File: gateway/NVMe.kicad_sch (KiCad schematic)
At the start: 27 parts, among them IC1501 ST1S14PHR, X1501 SSD

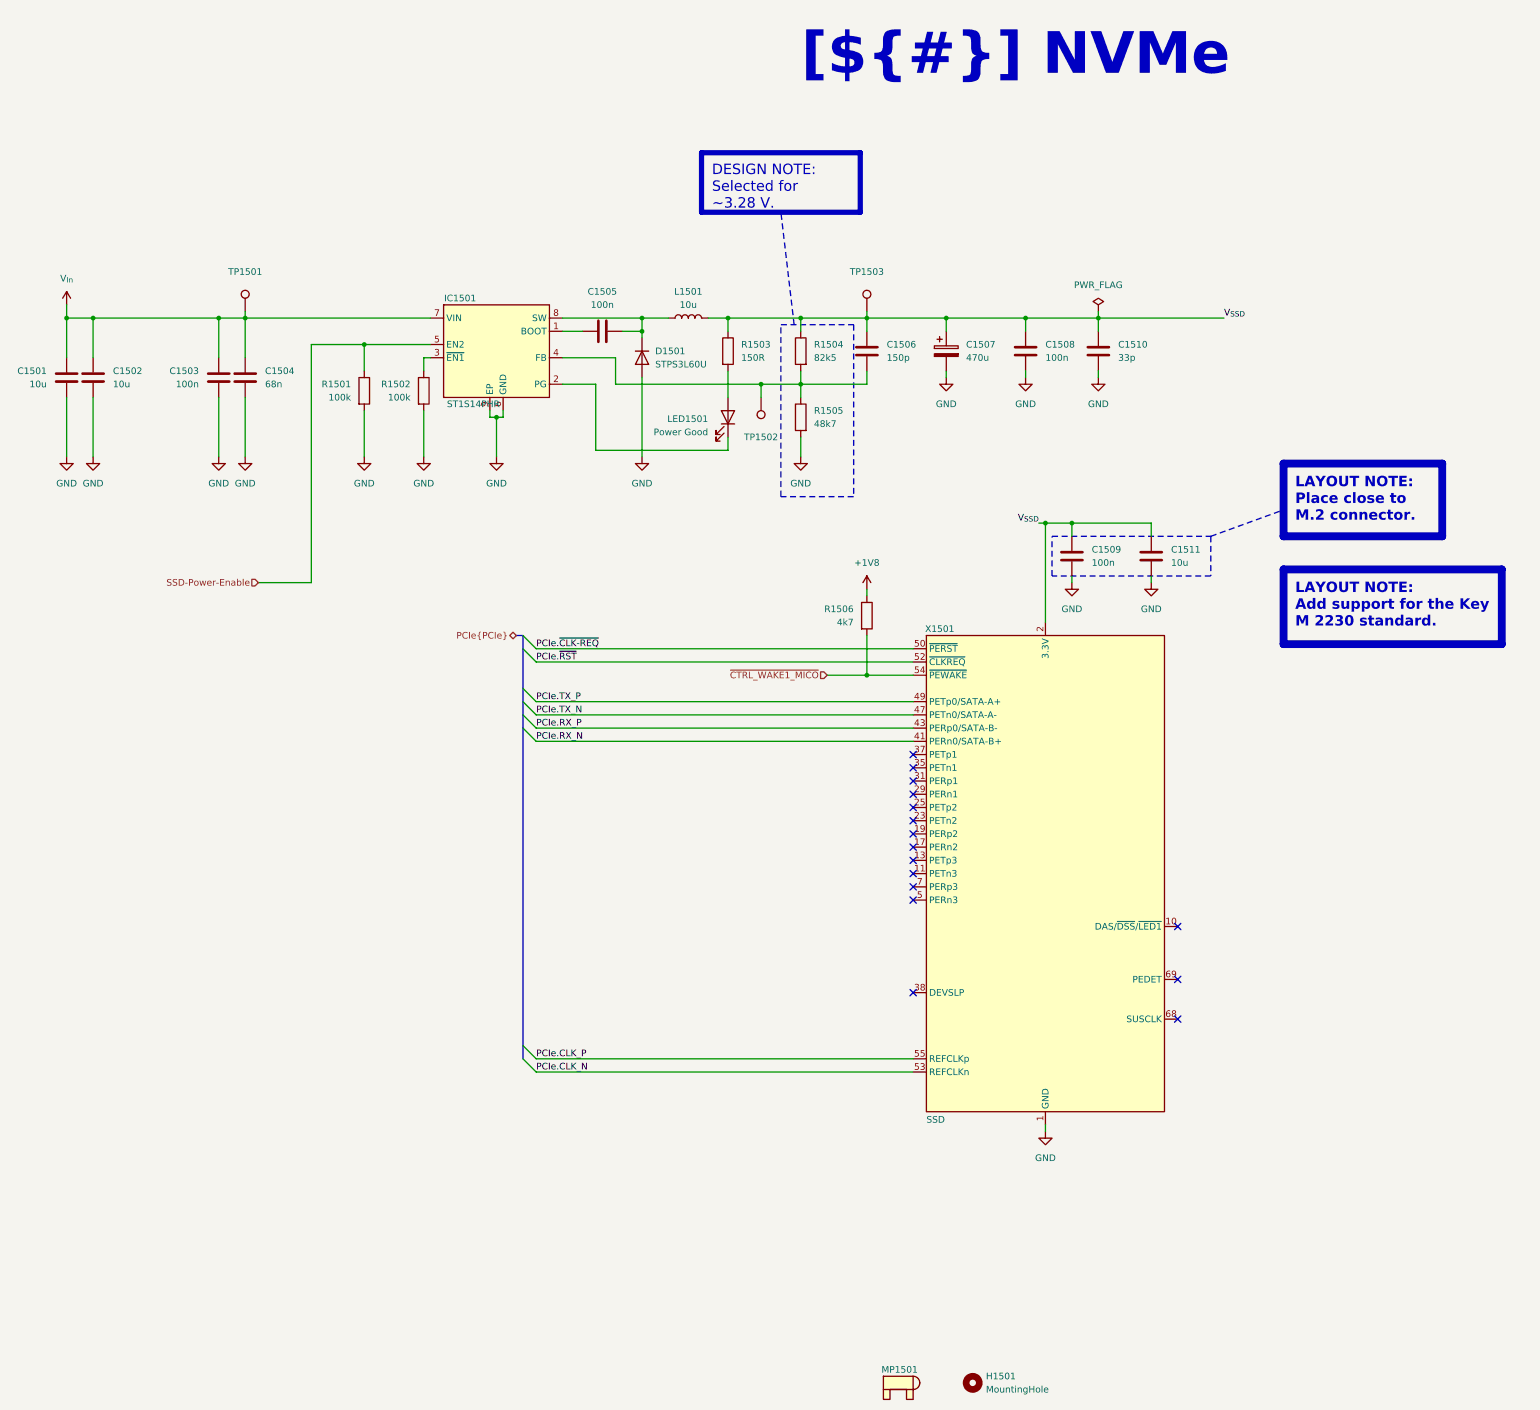
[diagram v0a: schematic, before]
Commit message: Add INA219 for current measurement
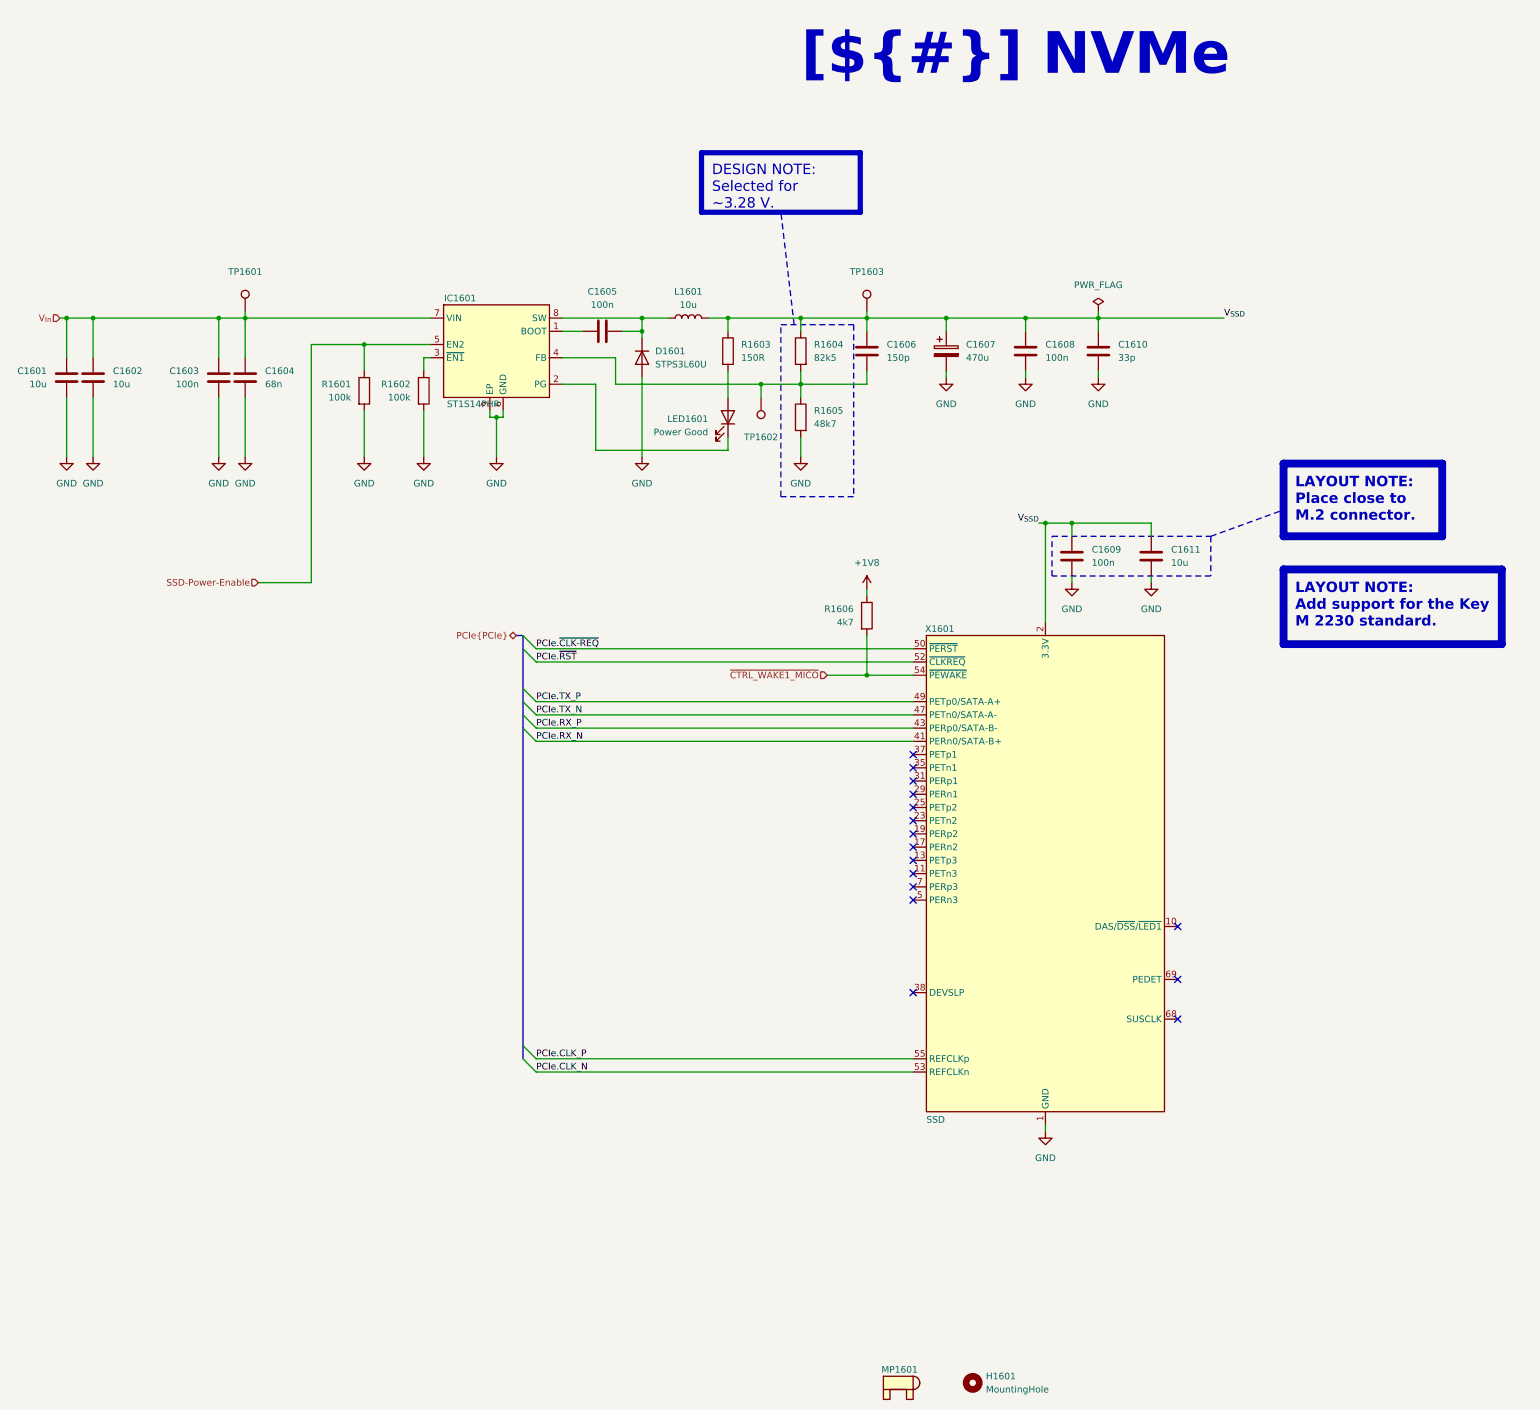
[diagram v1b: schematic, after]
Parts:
- renumbered C1501 to C1601, C1502 to C1602, C1503 to C1603, C1504 to C1604, C1505 to C1605, C1506 to C1606, C1507 to C1607, C1508 to C1608, C1509 to C1609, C1510 to C1610, C1511 to C1611, D1501 to D1601, H1501 to H1601, IC1501 to IC1601, L1501 to L1601, LED1501 to LED1601, MP1501 to MP1601, R1501 to R1601, R1502 to R1602, R1503 to R1603, R1504 to R1604, R1505 to R1605, R1506 to R1606, TP1501 to TP1601, TP1502 to TP1602, TP1503 to TP1603, X1501 to X1601

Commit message: Improving Thread
- Add boot signal for Thread MCU
- Add debug LED for nRF5340
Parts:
- C1610: manf# 0805YA330JAT2A -> 08053C330KAT2A
- TP1601, TP1602, TP1603: value ~ -> (none)
- X1601: manf# MDT420B03001 -> MDT420M03001; mouser# 523-MDT420B03001 -> 523-MDT420M03001
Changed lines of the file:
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@@
 			)
 		)
-		(property "manf#" "0805YA330JAT2A"
+		(property "manf#" "08053C330KAT2A"
 			(at 226.06 80.01 0)
 			(hide yes)
@@
 			)
 		)
-		(property "Value" "~"
+		(property "Value" ""
 			(at 161.29 94.615 0)
 			(show_name no)
@@
 			)
 		)
-		(property "manf#" "MDT420B03001"
+		(property "manf#" "MDT420M03001"
 			(at 215.9 180.34 0)
 			(hide yes)
@@
 			)
 		)
-		(property "mouser#" "523-MDT420B03001"
+		(property "mouser#" "523-MDT420M03001"
 			(at 215.9 180.34 0)
 			(hide yes)
@@
 			)
 		)
-		(property "Value" "~"
+		(property "Value" ""
 			(at 62.23 66.675 0)
 			(show_name no)
@@
 			)
 		)
-		(property "Datasheet" "https://datasheets.kyocera-avx.com/KGM_X7R.pdf"
+		(property "Datasheet" "https://datasheets.kyocera-avx.com/AutoMLCC.pdf"
 			(at 130.81 76.2 0)
 			(hide yes)
@@
 			)
 		)
-		(property "Datasheet" "https://datasheets.kyocera-avx.com/KGM_X7R.pdf"
+		(property "Datasheet" "https://datasheets.kyocera-avx.com/AutoMLCC.pdf"
 			(at 220.98 119.38 0)
 			(hide yes)
@@
 			)
 		)
-		(property "Datasheet" "https://datasheets.kyocera-avx.com/KGM_X7R.pdf"
+		(property "Datasheet" "https://datasheets.kyocera-avx.com/AutoMLCC.pdf"
 			(at 57.15 85.09 0)
 			(hide yes)
@@
 			)
 		)
-		(property "Value" "~"
+		(property "Value" ""
 			(at 181.61 66.675 0)
 			(show_name no)
@@
 			)
 		)
-		(property "Datasheet" "https://datasheets.kyocera-avx.com/KGM_X7R.pdf"
+		(property "Datasheet" "https://datasheets.kyocera-avx.com/AutoMLCC.pdf"
 			(at 212.09 80.01 0)
 			(hide yes)

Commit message: Working on PCB
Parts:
- removed LED1601: Power Good, LED_SMD:LED_0805_2012Metric, symbol Device:LED
- removed R1602: 100k, Resistor_SMD:R_0805_2012Metric, symbol Device:R
- removed R1603: 150R, Resistor_SMD:R_0805_2012Metric, symbol Device:R
- added R1607: 100k, Resistor_SMD:R_0805_2012Metric, symbol Device:R
- C1603, C1605, C1608, C1609: mouser# 581-04025C104JAT2A -> 581-08053C104M4T4A
- C1604: manf# 0805YC683KAT2A -> 08055C683K4T4A; mouser# 581-04025C683KAT2A -> 581-08055C683K4T4A
- C1606: mouser# 581-04025C151MAT2A -> 581-08051U151JAT2A
- C1610: mouser# 581-04021A330JAT2A -> 581-08053C330KAT2A
- R1601: mouser# 652-CR0402-JW-104GLF -> 652-CR0805-JW-104GLF
- R1604: manf# CR0805-JW-8252GLF -> CR0805-FX-8252ELF; mouser# 652-CR0402-FX-8252GLF -> 652-CR0805FX-8252ELF
- R1605: manf# CR0805-JW-4872GLF -> CR0805-FX-4872ELF; mouser# 652-CR0402-FX-4872GLF -> 652-CR0805-FX-4872ELF
- TP1601, TP1602, TP1603: value (none) -> ~
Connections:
- net GND: now also R1601.1, R1607.1; no longer R1601.2
- net SSD-Power-Enable: now also R1607.2; no longer R1601.1
- net at IC1601.3 (~{EN1}): now also R1601.2
- net at D1601.1 (K), IC1601.8 (SW), L1601.1: now also C1605.2; no longer C1605.1
- net at IC1601.1 (BOOT): now also C1605.1; no longer C1605.2
- no-connect marks 16 -> 17
